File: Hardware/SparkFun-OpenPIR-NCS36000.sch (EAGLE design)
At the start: 35 parts, among them U1 NCS36000, U2 PIR

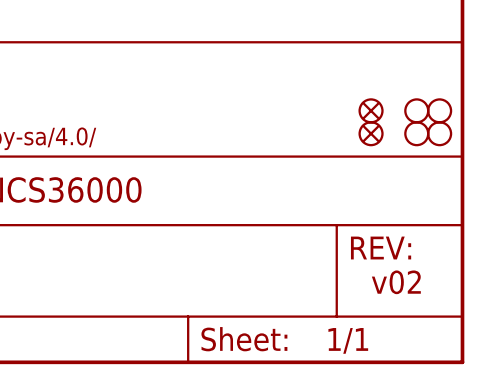
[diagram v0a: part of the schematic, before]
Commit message: Minor silkscreen adjustments. Incrementing to v10.
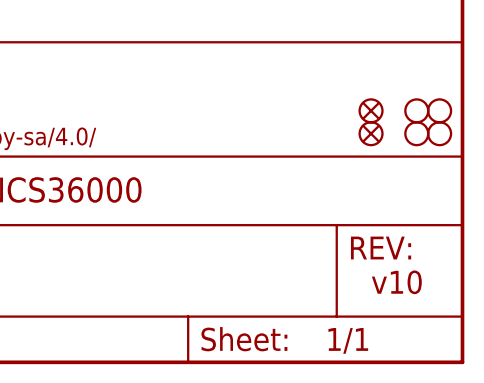
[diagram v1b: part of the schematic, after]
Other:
- note added: "v10"
- note removed: "v02"
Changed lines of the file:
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@@
 within 312 clock cycles.</text>
 <text x="170.18" y="7.62" size="2.54" layer="94" font="vector" ratio="10">Jim Lindblom</text>
-<text x="238.76" y="7.62" size="2.54" layer="94" font="vector" ratio="10">v02</text>
+<text x="238.76" y="7.62" size="2.54" layer="94" font="vector" ratio="10">v10</text>
 <text x="7.62" y="144.78" size="2.54" layer="97" font="vector" ratio="10">VCC Range: 3.0 - 5.75V</text>
 <text x="25.4" y="55.88" size="1.778" layer="97" font="vector">The NCS36000 features a 2-stage amplifier - gain and passband
